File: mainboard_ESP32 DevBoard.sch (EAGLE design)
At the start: 42 parts, among them IC1 LM358N, IC2 LM833N, IC3 74HC08N, K1 AQH213, X1 JST-XH-02-PIN-LONG-PAD, X2 JST-XH-04-PIN-LONG-PAD, X3 1751248, X4 1751248, X5 JST-XH-04-PIN-LONG-PAD

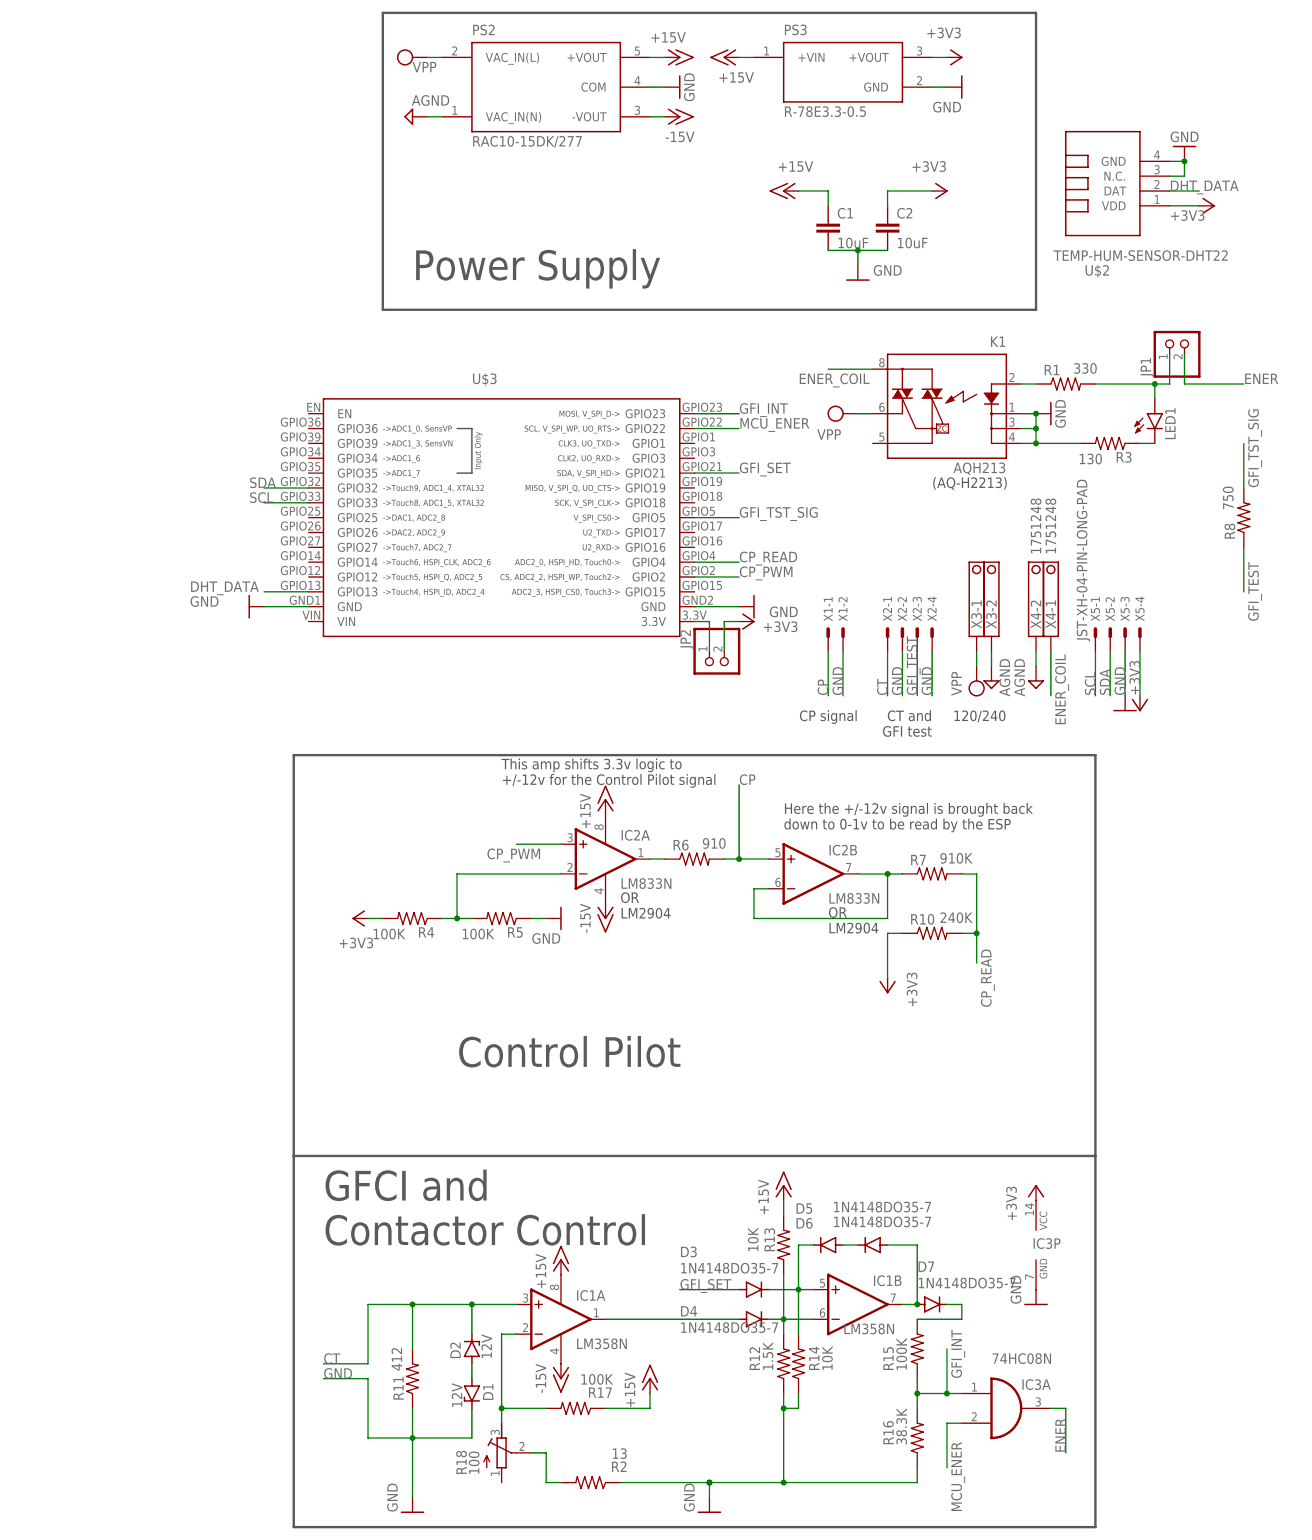
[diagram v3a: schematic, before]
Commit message: Made all traces as big as possible. Pads also. Added some layers for CAM outputs. Added cam job file
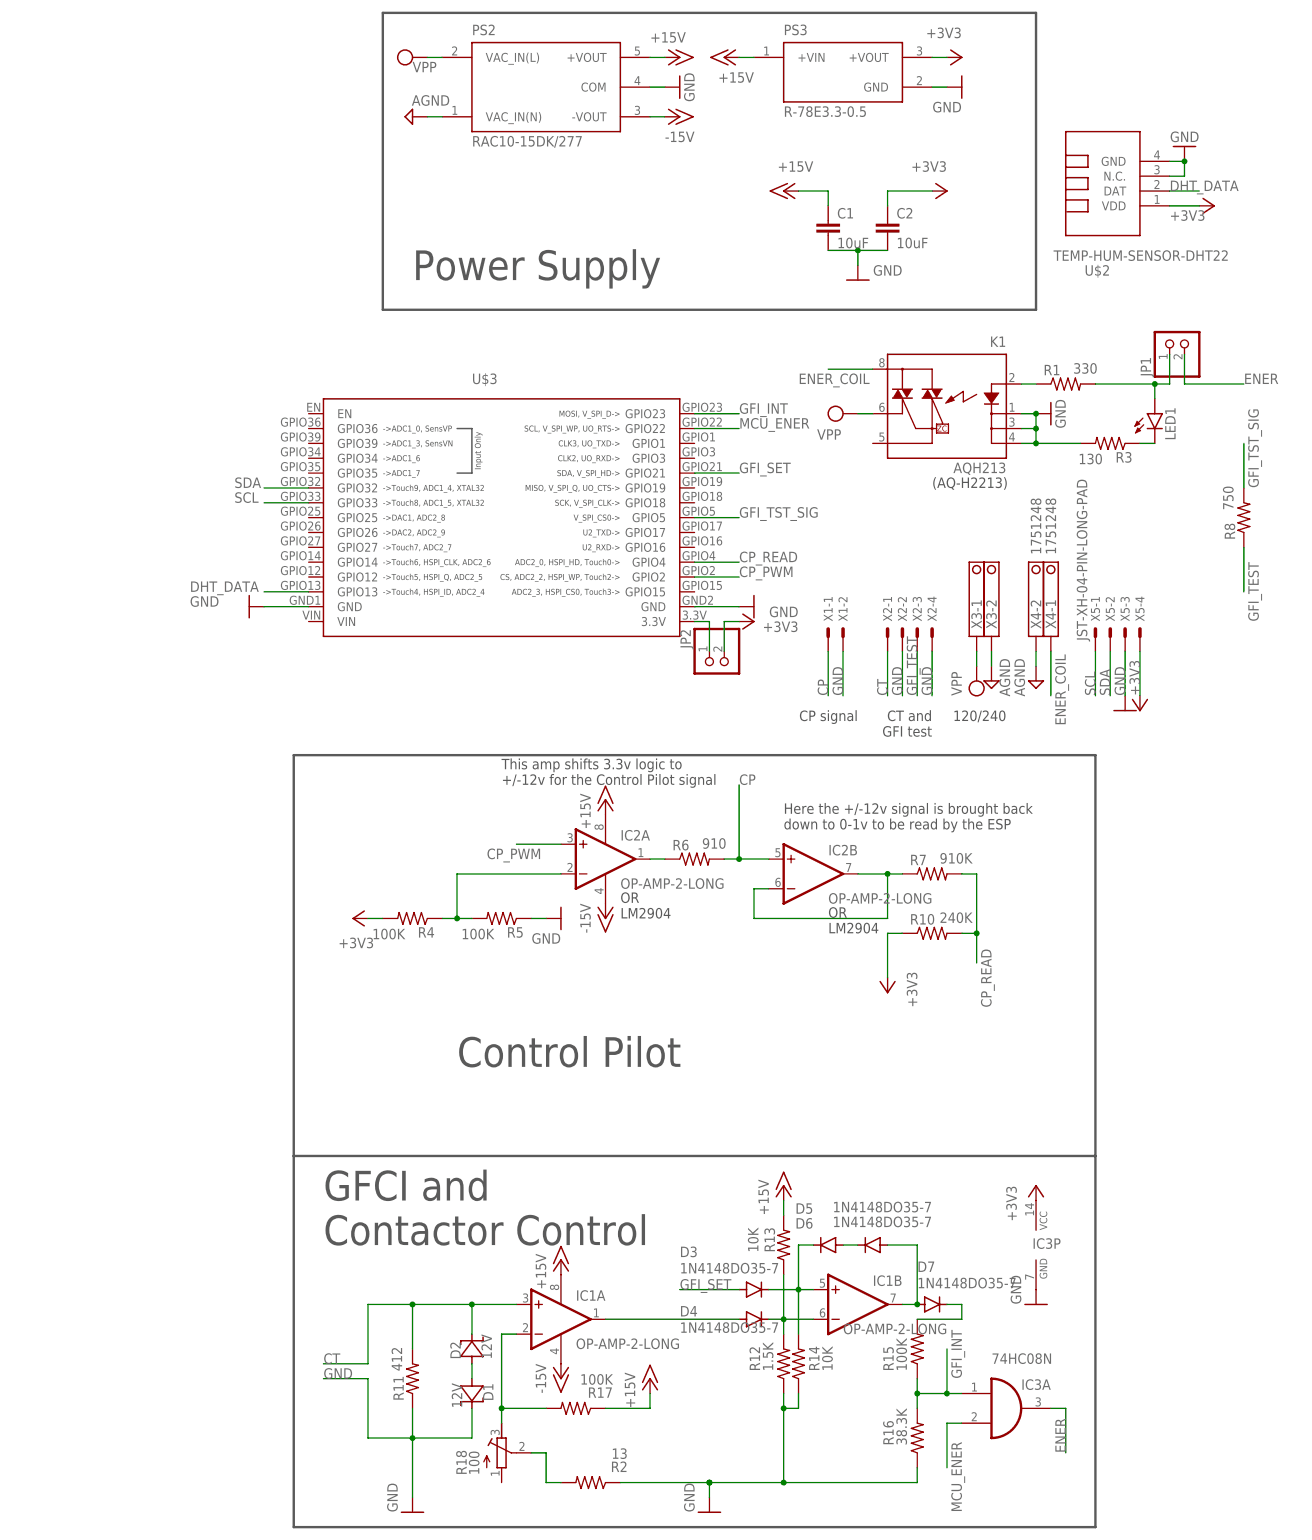
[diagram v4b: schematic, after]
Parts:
- D1, D2: device diode:ZENER-DIODEZD-7.5 -> Passive:ZENER
- IC1: value LM358N -> OP-AMP-2-LONG; device linear:LM358N -> Op Amp:OP-AMP-2-LONG
- IC2: value LM833N -> OP-AMP-2-LONG; device linear:LM833N -> Op Amp:OP-AMP-2-LONG
- R1, R10, R11, R12, R13, R14, R15, R16, R17, R2, R3, R4, R5, R6, R7, R8: device rcl:R-US_0204/7 -> Passive:RESISTORL
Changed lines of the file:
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@@
 <part name="SUPPLY1" library="supply2" library_urn="urn:adsk.eagle:library:372" deviceset="VPP" device=""/>
 <part name="SUPPLY2" library="supply2" library_urn="urn:adsk.eagle:library:372" deviceset="AGND" device=""/>
-<part name="R1" library="rcl" library_urn="urn:adsk.eagle:library:334" deviceset="R-US_" device="0204/7" package3d_urn="urn:adsk.eagle:package:23498/2" value="330"/>
+<part name="R1" library="Passive" deviceset="RESISTOR" device="L" value="330"/>
 <part name="U$2" library="diy-modules" deviceset="TEMP-HUM-SENSOR-DHT22" device=""/>
 <part name="GND1" library="supply1" library_urn="urn:adsk.eagle:library:371" deviceset="GND" device=""/>
@@
 <part name="P+2" library="supply1" library_urn="urn:adsk.eagle:library:371" deviceset="+15V" device=""/>
 <part name="P-1" library="supply1" library_urn="urn:adsk.eagle:library:371" deviceset="-15V" device=""/>
-<part name="IC2" library="linear" library_urn="urn:adsk.eagle:library:262" deviceset="LM833" device="N" package3d_urn="urn:adsk.eagle:package:16409/2"/>
+<part name="IC2" library="Op Amp" deviceset="OP-AMP-2" device="-LONG"/>
 <part name="P+3" library="supply1" library_urn="urn:adsk.eagle:library:371" deviceset="+15V" device=""/>
 <part name="P-2" library="supply1" library_urn="urn:adsk.eagle:library:371" deviceset="-15V" device=""/>
 <part name="+3V4" library="supply1" library_urn="urn:adsk.eagle:library:371" deviceset="+3V3" device=""/>
-<part name="R4" library="rcl" library_urn="urn:adsk.eagle:library:334" deviceset="R-US_" device="0204/7" package3d_urn="urn:adsk.eagle:package:23498/2" value="100K"/>
-<part name="R5" library="rcl" library_urn="urn:adsk.eagle:library:334" deviceset="R-US_" device="0204/7" package3d_urn="urn:adsk.eagle:package:23498/2" value="100K"/>
+<part name="R4" library="Passive" deviceset="RESISTOR" device="L" value="100K"/>
+<part name="R5" library="Passive" deviceset="RESISTOR" device="L" value="100K"/>
 <part name="GND8" library="supply1" library_urn="urn:adsk.eagle:library:371" deviceset="GND" device=""/>
-<part name="R6" library="rcl" library_urn="urn:adsk.eagle:library:334" deviceset="R-US_" device="0204/7" package3d_urn="urn:adsk.eagle:package:23498/2" value="910"/>
-<part name="R7" library="rcl" library_urn="urn:adsk.eagle:library:334" deviceset="R-US_" device="0204/7" package3d_urn="urn:adsk.eagle:package:23498/2" value="910K"/>
-<part name="R10" library="rcl" library_urn="urn:adsk.eagle:library:334" deviceset="R-US_" device="0204/7" package3d_urn="urn:adsk.eagle:package:23498/2" value="240K"/>
+<part name="R6" library="Passive" deviceset="RESISTOR" device="L" value="910"/>
+<part name="R7" library="Passive" deviceset="RESISTOR" device="L" value="910K"/>
+<part name="R10" library="Passive" deviceset="RESISTOR" device="L" value="240K"/>
 <part name="+3V6" library="supply1" library_urn="urn:adsk.eagle:library:371" deviceset="+3V3" device=""/>
 <part name="+3V3" library="supply1" library_urn="urn:adsk.eagle:library:371" deviceset="+3V3" device=""/>
@@
 <part name="C1" library="rcl" library_urn="urn:adsk.eagle:library:334" deviceset="C-EU" device="025-025X050" package3d_urn="urn:adsk.eagle:package:23629/2" value="10uF"/>
 <part name="C2" library="rcl" library_urn="urn:adsk.eagle:library:334" deviceset="C-EU" device="025-025X050" package3d_urn="urn:adsk.eagle:package:23629/2" value="10uF"/>
-<part name="D1" library="diode" library_urn="urn:adsk.eagle:library:210" deviceset="ZENER-DIODE" device="ZD-7.5" package3d_urn="urn:adsk.eagle:package:43411/1" value="12V"/>
-<part name="D2" library="diode" library_urn="urn:adsk.eagle:library:210" deviceset="ZENER-DIODE" device="ZD-7.5" package3d_urn="urn:adsk.eagle:package:43411/1" value="12V"/>
-<part name="IC1" library="linear" library_urn="urn:adsk.eagle:library:262" deviceset="LM358" device="N" package3d_urn="urn:adsk.eagle:package:16409/2"/>
-<part name="R11" library="rcl" library_urn="urn:adsk.eagle:library:334" deviceset="R-US_" device="0204/7" package3d_urn="urn:adsk.eagle:package:23498/2" value="412"/>
+<part name="D1" library="Passive" deviceset="ZENER" device="" value="12V"/>
+<part name="D2" library="Passive" deviceset="ZENER" device="" value="12V"/>
+<part name="IC1" library="Op Amp" deviceset="OP-AMP-2" device="-LONG"/>
+<part name="R11" library="Passive" deviceset="RESISTOR" device="L" value="412"/>
 <part name="D3" library="diode" library_urn="urn:adsk.eagle:library:210" deviceset="1N4148" device="DO35-7" package3d_urn="urn:adsk.eagle:package:43339/2"/>
 <part name="D4" library="diode" library_urn="urn:adsk.eagle:library:210" deviceset="1N4148" device="DO35-7" package3d_urn="urn:adsk.eagle:package:43339/2"/>
 <part name="D5" library="diode" library_urn="urn:adsk.eagle:library:210" deviceset="1N4148" device="DO35-7" package3d_urn="urn:adsk.eagle:package:43339/2"/>
 <part name="D6" library="diode" library_urn="urn:adsk.eagle:library:210" deviceset="1N4148" device="DO35-7" package3d_urn="urn:adsk.eagle:package:43339/2"/>
-<part name="R12" library="rcl" library_urn="urn:adsk.eagle:library:334" deviceset="R-US_" device="0204/7" package3d_urn="urn:adsk.eagle:package:23498/2" value="1.5K"/>
-<part name="R13" library="rcl" library_urn="urn:adsk.eagle:library:334" deviceset="R-US_" device="0204/7" package3d_urn="urn:adsk.eagle:package:23498/2" value="10K"/>
-<part name="R14" library="rcl" library_urn="urn:adsk.eagle:library:334" deviceset="R-US_" device="0204/7" package3d_urn="urn:adsk.eagle:package:23498/2" value="10K"/>
+<part name="R12" library="Passive" deviceset="RESISTOR" device="L" value="1.5K"/>
+<part name="R13" library="Passive" deviceset="RESISTOR" device="L" value="10K"/>
+<part name="R14" library="Passive" deviceset="RESISTOR" device="L" value="10K"/>
 <part name="IC3" library="74xx-eu" library_urn="urn:adsk.eagle:library:85" deviceset="74*08" device="N" package3d_urn="urn:adsk.eagle:package:16407/2" technology="HC"/>
-<part name="R15" library="rcl" library_urn="urn:adsk.eagle:library:334" deviceset="R-US_" device="0204/7" package3d_urn="urn:adsk.eagle:package:23498/2" value="100K"/>
-<part name="R16" library="rcl" library_urn="urn:adsk.eagle:library:334" deviceset="R-US_" device="0204/7" package3d_urn="urn:adsk.eagle:package:23498/2" value="38.3K"/>
+<part name="R15" library="Passive" deviceset="RESISTOR" device="L" value="100K"/>
+<part name="R16" library="Passive" deviceset="RESISTOR" device="L" value="38.3K"/>
 <part name="GND14" library="supply1" library_urn="urn:adsk.eagle:library:371" deviceset="GND" device=""/>
 <part name="+3V7" library="supply1" library_urn="urn:adsk.eagle:library:371" deviceset="+3V3" device=""/>
-<part name="R17" library="rcl" library_urn="urn:adsk.eagle:library:334" deviceset="R-US_" device="0204/7" package3d_urn="urn:adsk.eagle:package:23498/2" value="100K"/>
+<part name="R17" library="Passive" deviceset="RESISTOR" device="L" value="100K"/>
 <part name="GND15" library="supply1" library_urn="urn:adsk.eagle:library:371" deviceset="GND" device=""/>
 <part name="R18" library="rcl" library_urn="urn:adsk.eagle:library:334" deviceset="R-TRIMM" device="64W" package3d_urn="urn:adsk.eagle:package:23748/1" value="100"/>
@@
 <part name="SUPPLY6" library="supply2" library_urn="urn:adsk.eagle:library:372" deviceset="AGND" device=""/>
 <part name="X4" library="con-phoenix-350" library_urn="urn:adsk.eagle:library:174" deviceset="1751248" device="" package3d_urn="urn:adsk.eagle:package:9395/1"/>
-<part name="R2" library="rcl" library_urn="urn:adsk.eagle:library:334" deviceset="R-US_" device="0204/7" package3d_urn="urn:adsk.eagle:package:23498/2" value="13"/>
+<part name="R2" library="Passive" deviceset="RESISTOR" device="L" value="13"/>
 <part name="GND3" library="supply1" library_urn="urn:adsk.eagle:library:371" deviceset="GND" device=""/>
 <part name="U$3" library="ESP32" deviceset="ESP32-DOIT-V1" device=""/>
@@
 <part name="GND4" library="supply1" library_urn="urn:adsk.eagle:library:371" deviceset="GND" device=""/>
 <part name="JP1" library="pinhead" library_urn="urn:adsk.eagle:library:325" deviceset="PINHD-1X2" device="" package3d_urn="urn:adsk.eagle:package:22435/2"/>
-<part name="R3" library="rcl" library_urn="urn:adsk.eagle:library:334" deviceset="R-US_" device="0204/7" package3d_urn="urn:adsk.eagle:package:23498/2" value="130"/>
+<part name="R3" library="Passive" deviceset="RESISTOR" device="L" value="130"/>
 <part name="P+5" library="supply1" library_urn="urn:adsk.eagle:library:371" deviceset="+15V" device=""/>
 <part name="P+6" library="supply1" library_urn="urn:adsk.eagle:library:371" deviceset="+15V" device=""/>
@@
 <part name="LED1" library="led" library_urn="urn:adsk.eagle:library:259" deviceset="LED" device="3MM" package3d_urn="urn:adsk.eagle:package:15797/1"/>
 <part name="JP2" library="pinhead" library_urn="urn:adsk.eagle:library:325" deviceset="PINHD-1X2" device="/90" package3d_urn="urn:adsk.eagle:package:22437/2"/>
-<part name="R8" library="rcl" library_urn="urn:adsk.eagle:library:334" deviceset="R-US_" device="0204/7" package3d_urn="urn:adsk.eagle:package:23498/2" value="750"/>
+<part name="R8" library="Passive" deviceset="RESISTOR" device="L" value="750"/>
 <part name="X5" library="Rembrandt Electronics - JST XH Connectors v1-0" deviceset="JST-XH-04-PIN" device="-LONG-PAD"/>
 <part name="GND7" library="supply1" library_urn="urn:adsk.eagle:library:371" deviceset="GND" device=""/>
@@
 <pinref part="U$3" gate="G$1" pin="GPIO32"/>
 <wire x1="-5.08" y1="71.12" x2="-12.7" y2="71.12" width="0.1524" layer="91"/>
-<label x="-15.24" y="71.12" size="1.778" layer="95"/>
+<label x="-17.78" y="71.12" size="1.778" layer="95"/>
 </segment>
 </net>
@@
 <pinref part="U$3" gate="G$1" pin="GPIO33"/>
 <wire x1="-5.08" y1="68.58" x2="-12.7" y2="68.58" width="0.1524" layer="91"/>
-<label x="-15.24" y="68.58" size="1.778" layer="95"/>
-</segment>
-<segment>
+<label x="-17.78" y="68.58" size="1.778" layer="95"/>
+</segment>
+<segment>
